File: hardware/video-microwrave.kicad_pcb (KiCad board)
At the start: 2 copper layers, 47 x 93.3 mm, 56 parts, among them J501 PJ301M-12, J502 PJ301M-12, J503 PJ301M-12, J504 PJ301M-12, J505 PJ301M-12, J506 PJ301M-12, J507 PJ301M-12, J508 PJ301M-12, P101 CONN_01X05, P102 CONN_01X05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

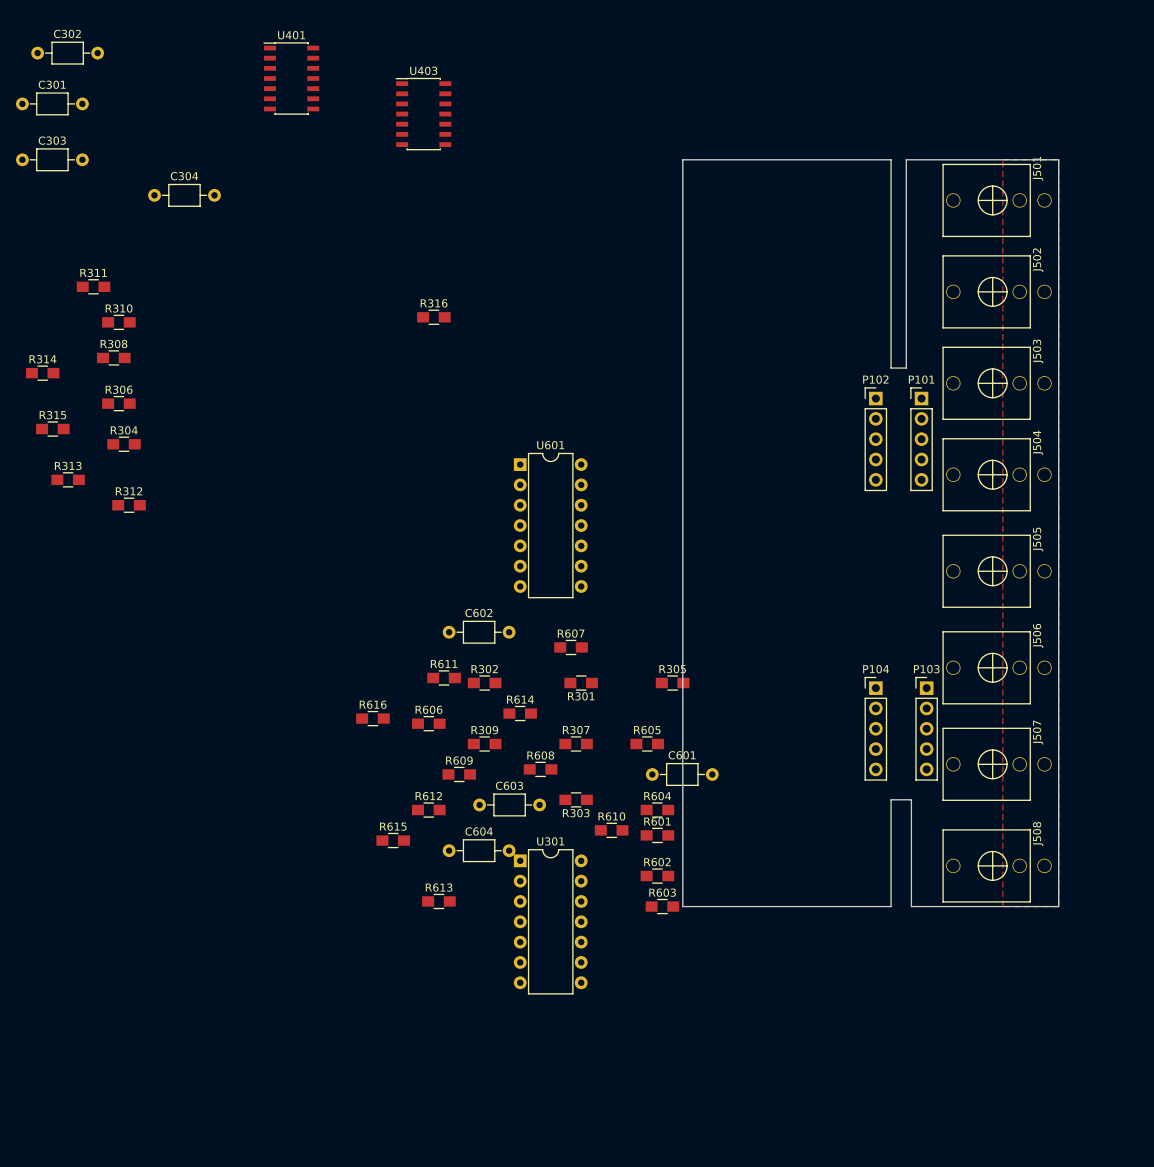
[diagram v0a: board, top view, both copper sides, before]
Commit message: most of the scematic is complete with the exception of the -5V offset
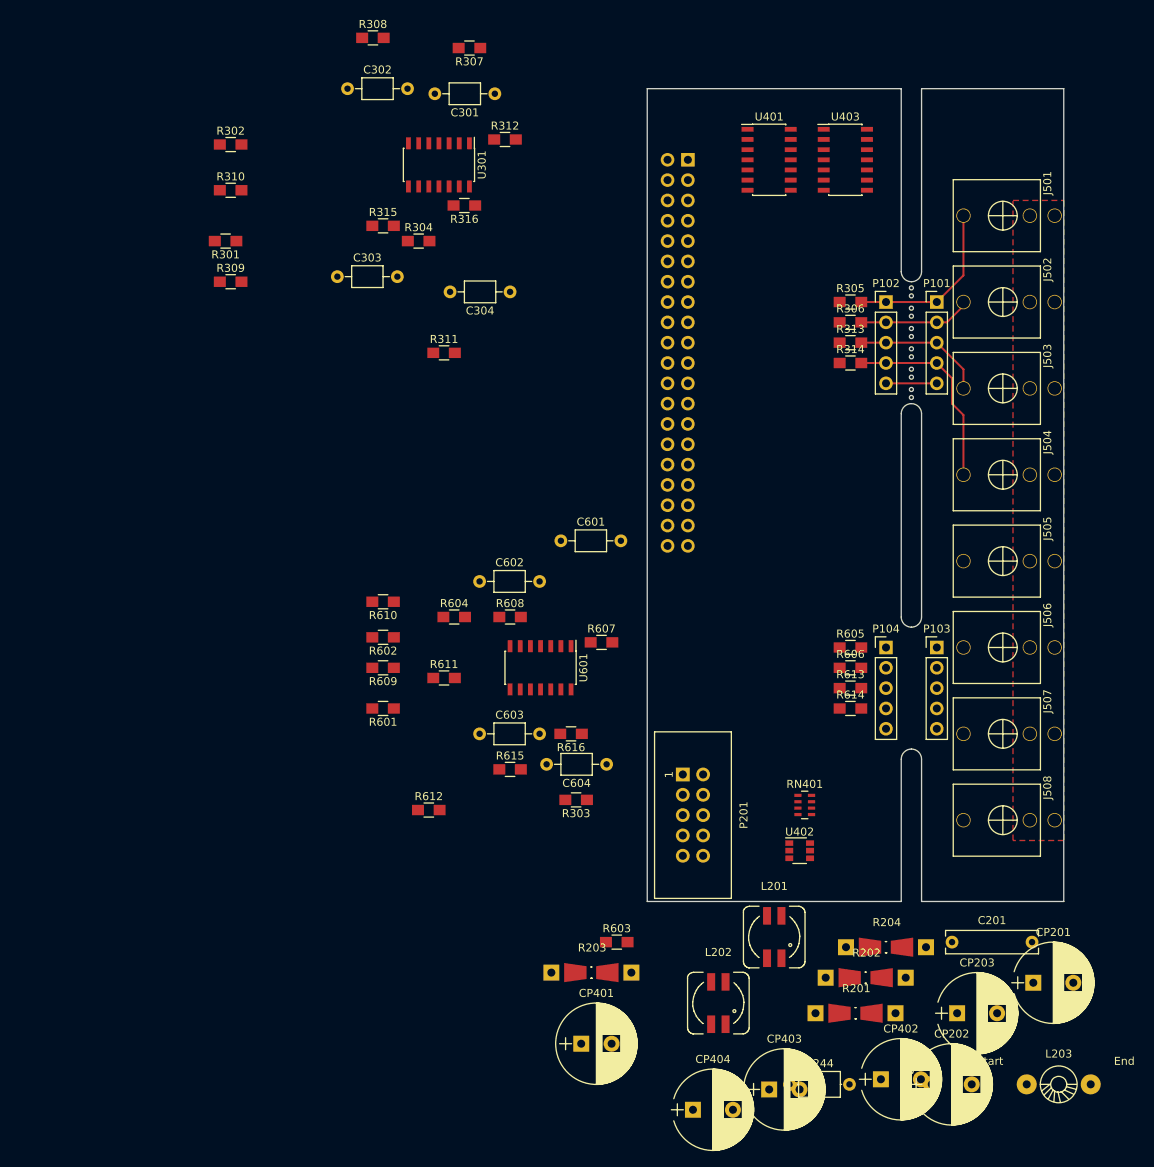
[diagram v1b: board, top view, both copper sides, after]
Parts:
- added C201: 1uF, Capacitors_THT:C_Rect_L11.5mm_W2.8mm_P10.00mm_MKT, F.Cu at (158.8, 144.8)
- added C244: 100nF, Capacitors_THT:C_Axial_L5.1mm_D3.1mm_P7.50mm_Horizontal, F.Cu at (138.4, 162.6)
- added CP201: 22uF, Capacitors_THT:CP_Radial_D10.0mm_P5.00mm, F.Cu at (168.9, 149.9)
- added CP202: 22uF, Capacitors_THT:CP_Radial_D10.0mm_P5.00mm, F.Cu at (156.2, 162.6)
- added CP203: 22uF, Capacitors_THT:CP_Radial_D10.0mm_P5.00mm, F.Cu at (159.4, 153.7)
- added CP401: 100nF, Capacitors_THT:CP_Radial_D10.0mm_P3.80mm, F.Cu at (112.4, 157.5)
- added CP402: 10uF, Capacitors_THT:CP_Radial_D10.0mm_P5.00mm, F.Cu at (149.9, 161.9)
- added CP403: 100nF, Capacitors_THT:CP_Radial_D10.0mm_P3.80mm, F.Cu at (135.9, 163.2)
- added CP404: 10uF, Capacitors_THT:CP_Radial_D10.0mm_P5.00mm, F.Cu at (126.4, 165.7)
- added L201: 100nH, Choke_SMD:Choke_Double_SMD_Wuerth-WE-DD-Typ-M-Typ-S, F.Cu at (136.5, 144.1)
- added L202: 100nH, Choke_SMD:Choke_Double_SMD_Wuerth-WE-DD-Typ-M-Typ-S, F.Cu at (129.5, 152.4)
- added L203: 6u8H, Choke_Toroid_ThroughHole:Choke_Toroid_horizontal_Diameter4-5mm_Amidon-T16, F.Cu at (172.1, 162.6)
- added MOUSEBITE1mm: VAL**, Microwrave:Mousebite_Mini_1mm, B.Cu at (153.7, 63.5)
- added MOUSEBITE1mm: VAL**, Microwrave:Mousebite_Mini_1mm, B.Cu at (153.7, 66.0)
- added MOUSEBITE1mm: VAL**, Microwrave:Mousebite_Mini_1mm, B.Cu at (153.7, 68.6)
- added MOUSEBITE1mm: VAL**, Microwrave:Mousebite_Mini_1mm, B.Cu at (153.7, 71.1)
- added MOUSEBITE1mm: VAL**, Microwrave:Mousebite_Mini_1mm, B.Cu at (153.7, 73.7)
- added MOUSEBITE1mm: VAL**, Microwrave:Mousebite_Mini_1mm, B.Cu at (153.7, 76.2)
- added P201: CONN_02X05, Connectors:IDC_Header_Straight_10pins, F.Cu at (125.1, 123.8)
- added R201: 100k, Resistors_Universal:Resistor_SMD+THTuniversal_0805to1206_RM10_HandSoldering_RevA_Date25Jun2010, F.Cu at (146.7, 153.7)
- added R202: 402k2, Resistors_Universal:Resistor_SMD+THTuniversal_0805to1206_RM10_HandSoldering_RevA_Date25Jun2010, F.Cu at (148.0, 149.2)
- added R203: 75k, Resistors_Universal:Resistor_SMD+THTuniversal_0805to1206_RM10_HandSoldering_RevA_Date25Jun2010, F.Cu at (113.7, 148.6)
- added R204: 7k68, Resistors_Universal:Resistor_SMD+THTuniversal_0805to1206_RM10_HandSoldering_RevA_Date25Jun2010, F.Cu at (150.5, 145.4)
- added RN401: 10k, Resistors_SMD:R_Array_Concave_4x0603, F.Cu at (140.3, 127.6)
- added U101: Raspberry_Pi_Zero, Pin_Headers:Pin_Header_Straight_2x20_Pitch2.54mm, B.Cu at (125.7, 47.0)
- added U402: FDC6301N, TO_SOT_Packages_SMD:SuperSOT-6, F.Cu at (139.7, 133.3)
- U301, U601: footprint Housings_DIP:DIP-14_W7.62mm -> Housings_SOIC:SOIC-14_3.9x8.7mm_Pitch1.27mm
- moved R314 101.0 mm to (146.1, 72.4)
- moved R313 99.3 mm to (146.1, 69.8)
- moved R306 92.0 mm to (146.1, 67.3)
- moved R307 88.0 mm to (98.4, 33.0), turned to 180 degrees
- moved U301 87.6 mm to (94.6, 47.6), turned to 270 degrees
- moved R302 74.4 mm to (68.6, 45.1)
- moved R301 70.9 mm to (67.9, 57.1)
- moved R309 65.9 mm to (68.6, 62.2)
- moved R312 65.6 mm to (102.9, 44.5)
- moved U401 60.5 mm to (135.9, 47.0)
- moved C301 59.1 mm to (101.6, 38.7), turned to 180 degrees
- moved R613 57.9 mm to (146.1, 113.0)
- moved R606 53.2 mm to (146.1, 110.5)
- moved U403 53.0 mm to (145.4, 47.0)
- moved R305 52.6 mm to (146.1, 64.8)
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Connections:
- R303 pad 1: (no net) -> /1
- R304 pad 1: (no net) -> /2
- R311 pad 1: (no net) -> /3
- R312 pad 1: (no net) -> /4
- R601 pad 2: /buffers 5-6/-5V -> /buffers 1-4/-5V
- R602 pad 2: /buffers 5-6/-5V -> /buffers 1-4/-5V
- R603 pad 1: (no net) -> /5
- R604 pad 1: (no net) -> /6
- R609 pad 2: /buffers 5-6/-5V -> /buffers 1-4/-5V
- R610 pad 2: /buffers 5-6/-5V -> /buffers 1-4/-5V
- R611 pad 1: (no net) -> /7
- R612 pad 1: (no net) -> /8
- U401 pad 1: (no net) -> /1
- U401 pad 10: (no net) -> +5V
- U401 pad 11: (no net) -> /3
- U401 pad 13: (no net) -> /4
- U401 pad 3: (no net) -> /2
- U401 pad 7: (no net) -> /adc/SDA_5V
- U401 pad 8: (no net) -> /adc/SCL_5V
- U401 pad 9: (no net) -> Earth
- U403 pad 1: (no net) -> /5
- U403 pad 10: (no net) -> Earth
- U403 pad 11: (no net) -> /8
- U403 pad 13: (no net) -> /7
- U403 pad 3: (no net) -> /6
- U403 pad 7: (no net) -> /adc/SDA_5V
- U403 pad 8: (no net) -> /adc/SCL_5V
- U403 pad 9: (no net) -> +5V
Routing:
- net /4: track 0.00 -> 24.8 mm
- net /1: track 0.00 -> 21.6 mm
- net /3: track 0.00 -> 16.5 mm
- net /2: track 0.00 -> 14.1 mm
- net Earth: track 0.00 -> 6.35 mm
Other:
- board size 47 x 93.3 mm -> 52.1 x 101.6 mm

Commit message: updated footprint & first tracks laid
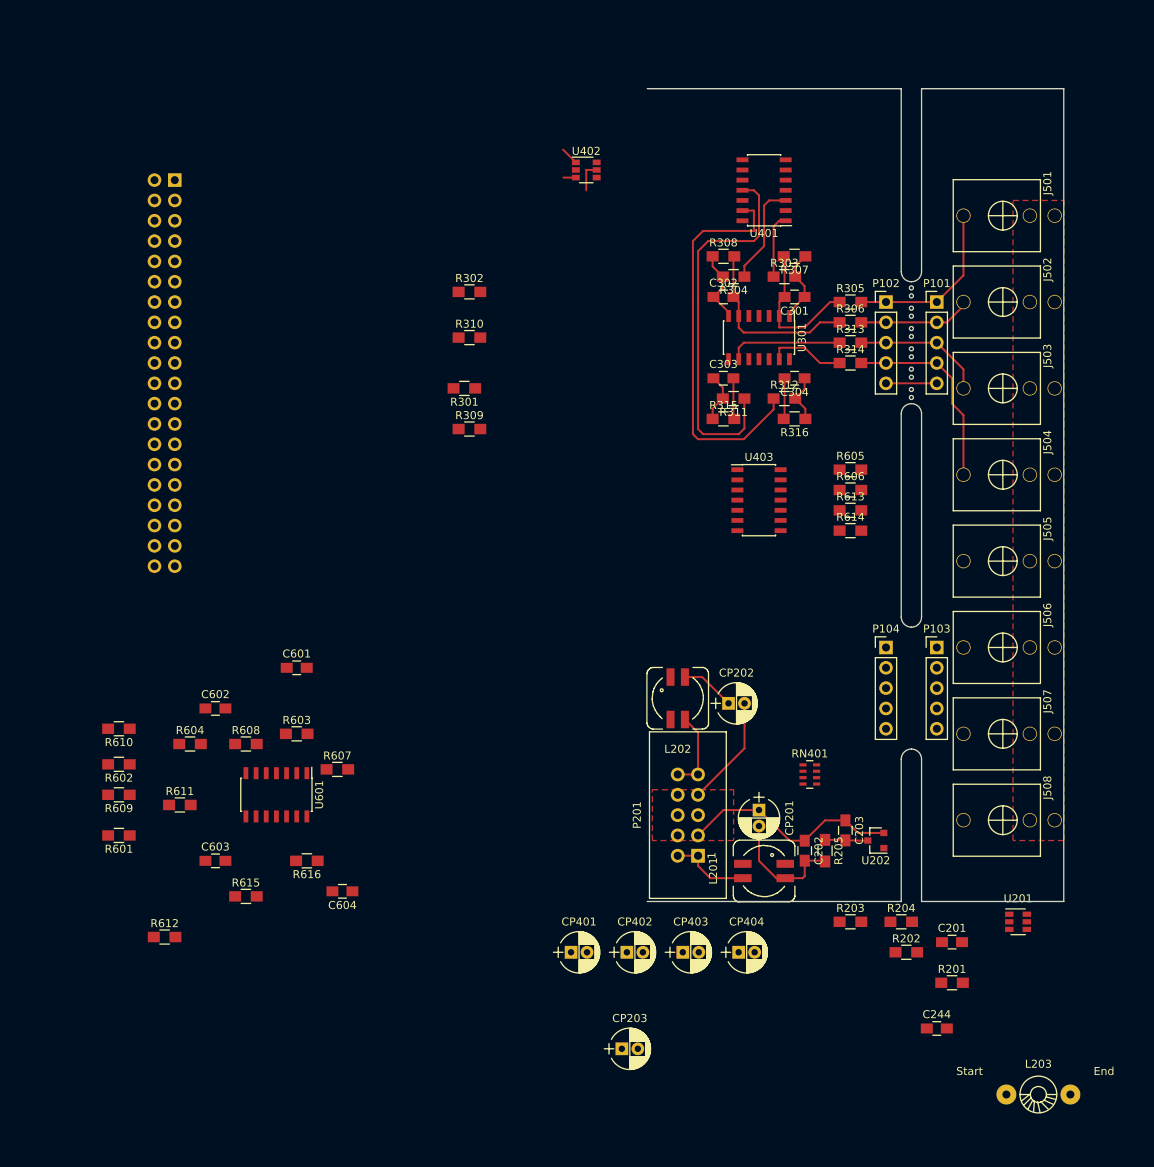
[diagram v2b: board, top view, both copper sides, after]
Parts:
- added C202: 1uF, Capacitors_SMD:C_0805_HandSoldering, F.Cu at (140.3, 133.3)
- added C203: 1uF, Capacitors_SMD:C_0805_HandSoldering, F.Cu at (145.4, 130.8)
- added R205: 2k, Resistors_SMD:R_0805_HandSoldering, F.Cu at (142.9, 133.3)
- added U201: MP1469, TO_SOT_Packages_SMD:SOT-23-6, F.Cu at (167.0, 142.2)
- added U202: NCP1117DT50G, TO_SOT_Packages_SMD:SOT-23, F.Cu at (149.2, 132.1)
- C201: footprint Capacitors_THT:C_Rect_L11.5mm_W2.8mm_P10.00mm_MKT -> Capacitors_SMD:C_0805_HandSoldering
- C244: footprint Capacitors_THT:C_Axial_L5.1mm_D3.1mm_P7.50mm_Horizontal -> Capacitors_SMD:C_0805_HandSoldering
- C301, C302, C303, C304, C601, C602, C603, C604: footprint Capacitors_THT:C_Axial_L3.8mm_D2.6mm_P7.50mm_Horizontal -> Capacitors_SMD:C_0805_HandSoldering
- CP201, CP202, CP203, CP402, CP404: footprint Capacitors_THT:CP_Radial_D10.0mm_P5.00mm -> Capacitors_THT:CP_Radial_D5.0mm_P2.00mm
- CP401, CP403: footprint Capacitors_THT:CP_Radial_D10.0mm_P3.80mm -> Capacitors_THT:CP_Radial_D5.0mm_P2.00mm
- R201, R202, R203, R204: footprint Resistors_Universal:Resistor_SMD+THTuniversal_0805to1206_RM10_HandSoldering_RevA_Date25Jun2010 -> Resistors_SMD:R_0805_HandSoldering
- moved U402 89.2 mm to (113.0, 48.3)
- moved R303 70.4 mm to (137.8, 61.6), turned to 0 degrees
- moved U101 64.2 mm to (61.6, 49.5)
- moved CP202 54.0 mm to (130.8, 114.9)
- moved C302 53.7 mm to (130.2, 64.1)
- moved R308 51.6 mm to (130.2, 59.1)
- moved C303 49.9 mm to (130.2, 74.3)
- moved R316 49.1 mm to (139.1, 79.4)
- moved R315 48.9 mm to (130.2, 79.4)
- moved R307 48.3 mm to (139.1, 59.1)
- moved R603 47.7 mm to (76.8, 118.7)
- moved R312 47.6 mm to (137.8, 76.8)
- moved U301 45.5 mm to (134.6, 69.2)
- moved C301 45.3 mm to (139.1, 64.1)
- moved U403 43.9 mm to (134.6, 89.5)
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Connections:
- J501 pad 3: /1 -> /cv1_raw
- J502 pad 3: /2 -> /cv2_raw
- J503 pad 3: /3 -> /cv3_raw
- J504 pad 3: /4 -> /cv4_raw
- J505 pad 3: /5 -> /cv5_raw
- J506 pad 3: /6 -> /cv6_raw
- J507 pad 3: /7 -> /cv7_raw
- J508 pad 3: /8 -> /cv8_raw
- P101 pad 1: /1 -> /cv1_raw
- P101 pad 2: /2 -> /cv2_raw
- P101 pad 3: /3 -> /cv3_raw
- P101 pad 4: /4 -> /cv4_raw
- P102 pad 1: /1 -> /cv1_raw
- P102 pad 2: /2 -> /cv2_raw
- P102 pad 3: /3 -> /cv3_raw
- P102 pad 4: /4 -> /cv4_raw
- P103 pad 1: /5 -> /cv5_raw
- P103 pad 2: /6 -> /cv6_raw
- P103 pad 3: /7 -> /cv7_raw
- P103 pad 4: /8 -> /cv8_raw
- P104 pad 1: /5 -> /cv5_raw
- P104 pad 2: /6 -> /cv6_raw
- P104 pad 3: /7 -> /cv7_raw
- P104 pad 4: /8 -> /cv8_raw
- R303 pad 1: /1 -> /buffered_1
- R304 pad 1: /2 -> /buffered_2
- R305 pad 2: /1 -> /cv1_raw
- R306 pad 2: /2 -> /cv2_raw
- R311 pad 1: /3 -> /buffered_3
- R312 pad 1: /4 -> /buffered_4
- R313 pad 2: /3 -> /cv3_raw
- R314 pad 2: /4 -> /cv4_raw
- R603 pad 1: /5 -> /buffered_5
- R604 pad 1: /6 -> /buffered_6
- R605 pad 2: /5 -> /cv5_raw
- R606 pad 2: /6 -> /cv6_raw
- R611 pad 1: /7 -> /buffered_7
- R612 pad 1: /8 -> /buffered_8
- R613 pad 2: /7 -> /cv7_raw
- R614 pad 2: /8 -> /cv8_raw
- U401 pad 1: /1 -> /buffered_1
- U401 pad 11: /3 -> /buffered_3
- U401 pad 13: /4 -> /buffered_4
- U401 pad 3: /2 -> /buffered_2
- U403 pad 1: /5 -> /buffered_5
- U403 pad 11: /8 -> /buffered_8
- U403 pad 13: /7 -> /buffered_7
- U403 pad 3: /6 -> /buffered_6
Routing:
- net /buffered_4: track 0.00 -> 49.5 mm
- net /buffered_3: track 0.00 -> 48.1 mm
- net Earth: track 6.35 -> 48.0 mm
- net /cv4_raw: track 0.00 -> 24.8 mm
- net /4: track 24.8 -> 0.00 mm
- net Net-(C302-Pad2): track 0.00 -> 22.8 mm
- net /cv1_raw: track 0.00 -> 21.6 mm
- net /1: track 21.6 -> 0.00 mm
- net Net-(C303-Pad2): track 0.00 -> 19.5 mm
- net Net-(C301-Pad2): track 0.00 -> 18.2 mm
- net /cv3_raw: track 0.00 -> 16.5 mm
- net /3: track 16.5 -> 0.00 mm
- net VEE: track 0.00 -> 16.4 mm
- net Net-(C304-Pad2): track 0.00 -> 14.9 mm
- net /cv2_raw: track 0.00 -> 14.1 mm
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
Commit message: finalized most footprints and nets.
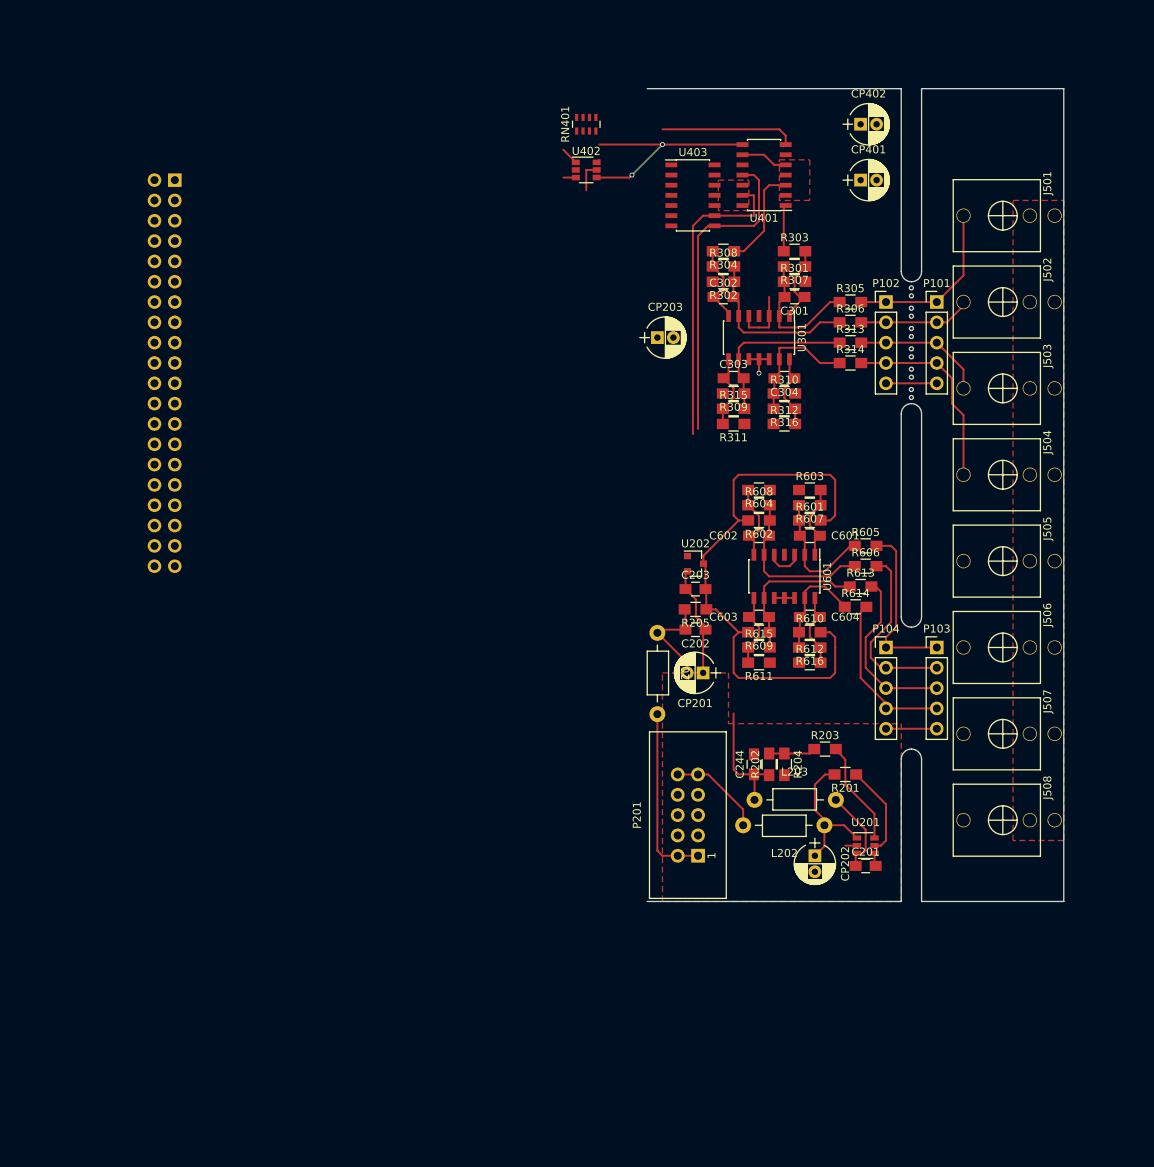
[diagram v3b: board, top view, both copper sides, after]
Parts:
- removed CP403: 100nF, Capacitors_THT:CP_Radial_D5.0mm_P2.00mm
- removed CP404: 10uF, Capacitors_THT:CP_Radial_D5.0mm_P2.00mm
- L201, L202: footprint Choke_SMD:Choke_Double_SMD_Wuerth-WE-DD-Typ-M-Typ-S -> Choke_Axial_ThroughHole:Choke_Horizontal_RM10mm
- L203: footprint Choke_Toroid_ThroughHole:Choke_Toroid_horizontal_Diameter4-5mm_Amidon-T16 -> Choke_Axial_ThroughHole:Choke_Horizontal_RM10mm
- moved CP402 107.5 mm to (147.3, 42.5)
- moved CP401 103.1 mm to (147.3, 49.5)
- moved R601 94.9 mm to (141.0, 92.1), turned to 0 degrees
- moved CP203 89.0 mm to (121.9, 69.2)
- moved R612 87.6 mm to (141.0, 109.9)
- moved R610 87.2 mm to (141.0, 106.0), turned to 0 degrees
- moved RN401 85.9 mm to (113.0, 42.5), turned to 90 degrees
- moved R602 85.6 mm to (134.6, 92.1)
- moved R609 82.5 mm to (134.6, 106.0)
- moved R604 77.9 mm to (134.6, 88.3), turned to 180 degrees
- moved R611 74.5 mm to (134.6, 109.9), turned to 180 degrees
- moved C603 74.5 mm to (134.6, 104.1)
- moved C602 71.3 mm to (134.6, 94.0)
- moved R615 71.3 mm to (134.6, 108.0)
- moved R603 71.0 mm to (141.0, 88.3)
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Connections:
- net Net-(L201-Pad2) renamed /power/-12
- net Net-(L202-Pad2) renamed /power/+12
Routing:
- net /buffers 1-4/-5V: track 5.38 -> 72.1 mm
- net /adc/SDA_5V: track 0.00 -> 26.8 mm, vias 0 -> 2
- net /cv6_raw: track 0.00 -> 22.7 mm
- net /cv7_raw: track 0.00 -> 21.7 mm
- net /cv5_raw: track 0.00 -> 21.7 mm
- net Net-(C602-Pad2): track 0.00 -> 21.2 mm
- net /cv8_raw: track 0.00 -> 20.7 mm
- net Net-(C603-Pad2): track 0.00 -> 19.2 mm
- net /adc/SCL_5V: track 0.00 -> 18.4 mm
- net Net-(C601-Pad2): track 0.00 -> 16.0 mm
- net +5V: track 0.00 -> 15.0 mm
- net Net-(C604-Pad2): track 0.00 -> 13.6 mm
- net Net-(R203-Pad2): track 0.00 -> 13.1 mm
- net /power/-12: track 10.1 -> 22.4 mm
- net Net-(R201-Pad1): track 0.00 -> 12.1 mm
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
